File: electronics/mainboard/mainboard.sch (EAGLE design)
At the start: 60 parts, among them CON1 B3B-ZR, IC1 TPS6300, IC2 TPS77033, J1 2MMPAD, J10 2MMPAD, J2 2MMPAD, J3 2MMPAD, J4 2MMPAD, J5 2MMPAD, J6 2MMPAD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

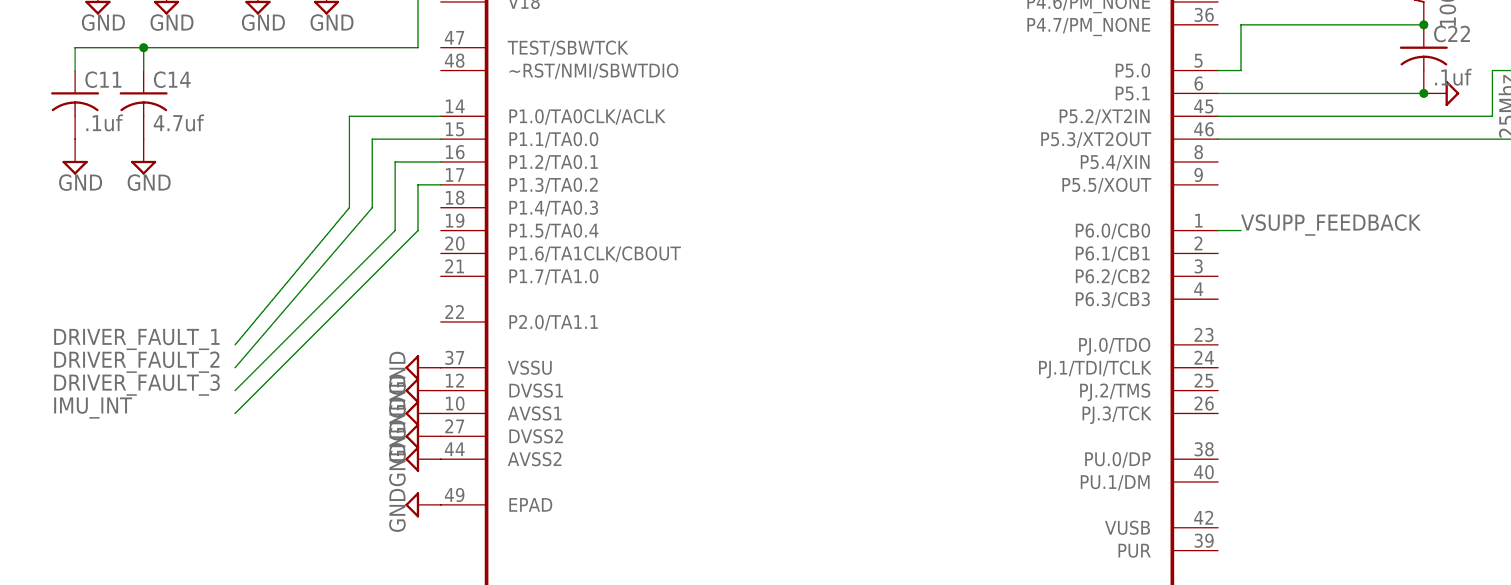
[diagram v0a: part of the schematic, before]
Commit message: renamed some files and cleaned up.  Added motordriver component
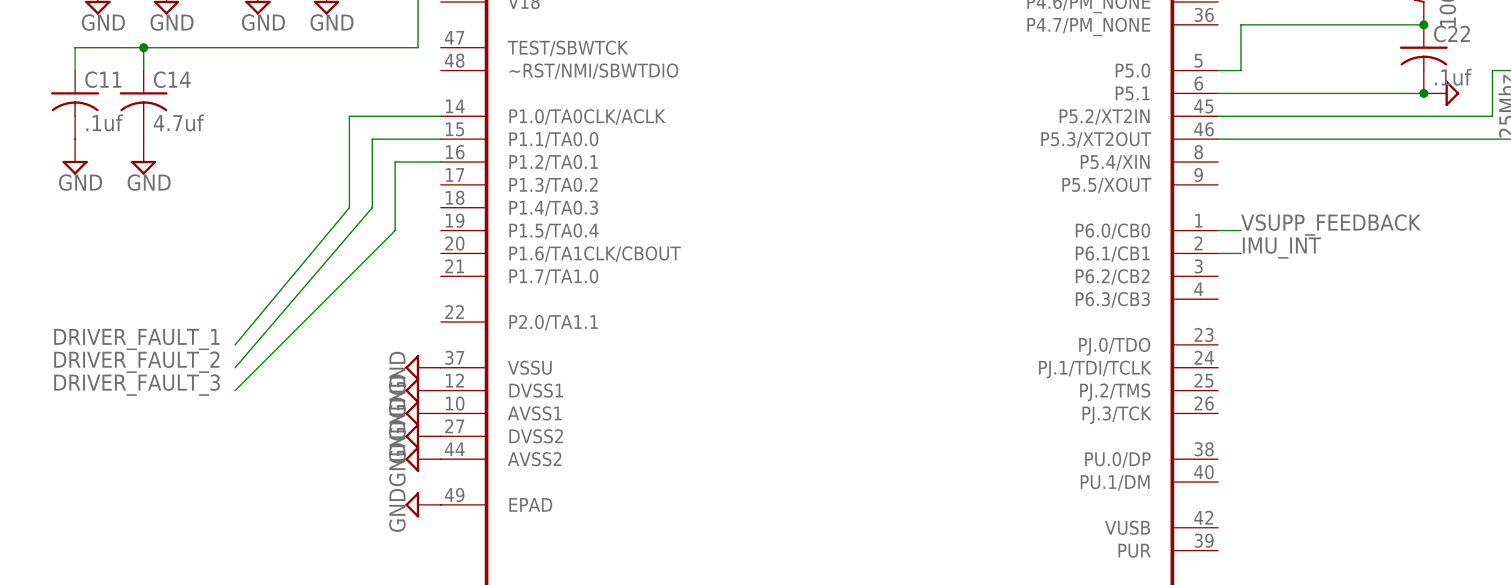
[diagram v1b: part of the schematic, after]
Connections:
- net IMU_INT: now also U2.P6.1/CB1; no longer U2.P1.3/TA0.2
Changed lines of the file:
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@@
 <?xml version="1.0" encoding="utf-8"?>
 <!DOCTYPE eagle SYSTEM "eagle.dtd">
-<eagle version="6.6.0">
+<eagle version="7.0.0">
 <drawing>
 <settings>
@@
 <label x="-12.7" y="-35.56" size="1.778" layer="95"/>
 <pinref part="U2" gate="A" pin="P1.2/TA0.1"/>
-<wire x1="25.4" y1="-10.16" x2="30.48" y2="-10.16" width="0.1524" layer="91"/>
+<wire x1="30.48" y1="-10.16" x2="25.4" y2="-10.16" width="0.1524" layer="91"/>
 </segment>
 </net>
@@
 </segment>
 <segment>
-<wire x1="27.94" y1="-12.7" x2="27.94" y2="-17.78" width="0.1524" layer="91"/>
-<wire x1="27.94" y1="-17.78" x2="7.62" y2="-38.1" width="0.1524" layer="91"/>
-<label x="-12.7" y="-38.1" size="1.778" layer="95"/>
-<pinref part="U2" gate="A" pin="P1.3/TA0.2"/>
-<wire x1="27.94" y1="-12.7" x2="30.48" y2="-12.7" width="0.1524" layer="91"/>
-</segment>
-</net>
+<label x="119.38" y="-20.32" size="1.778" layer="95"/>
+<pinref part="U2" gate="A" pin="P6.1/CB1"/>
+<wire x1="119.38" y1="-20.32" x2="116.84" y2="-20.32" width="0.1524" layer="91"/>
+</segment>
+</net>

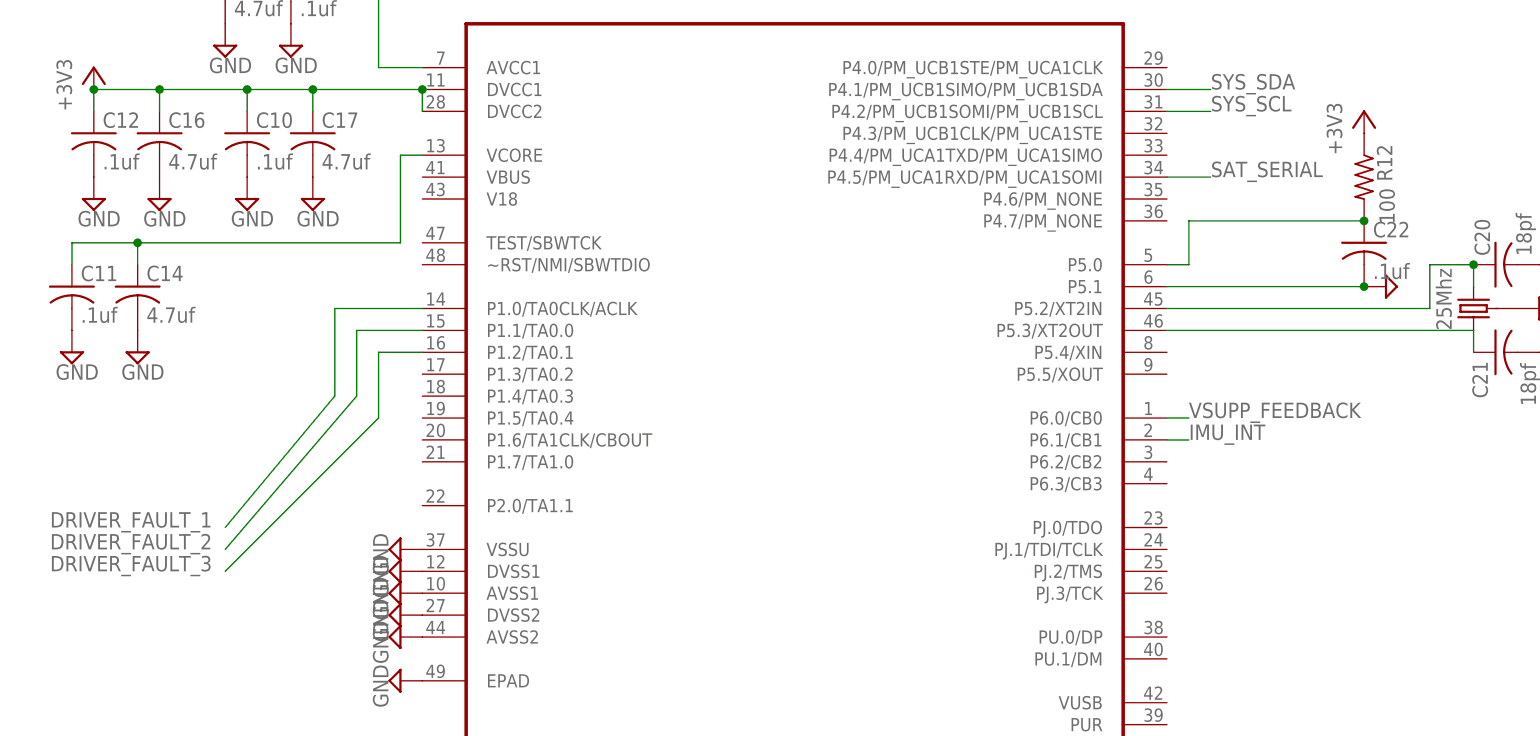
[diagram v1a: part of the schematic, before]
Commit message: layout mostly done, need to add programming header
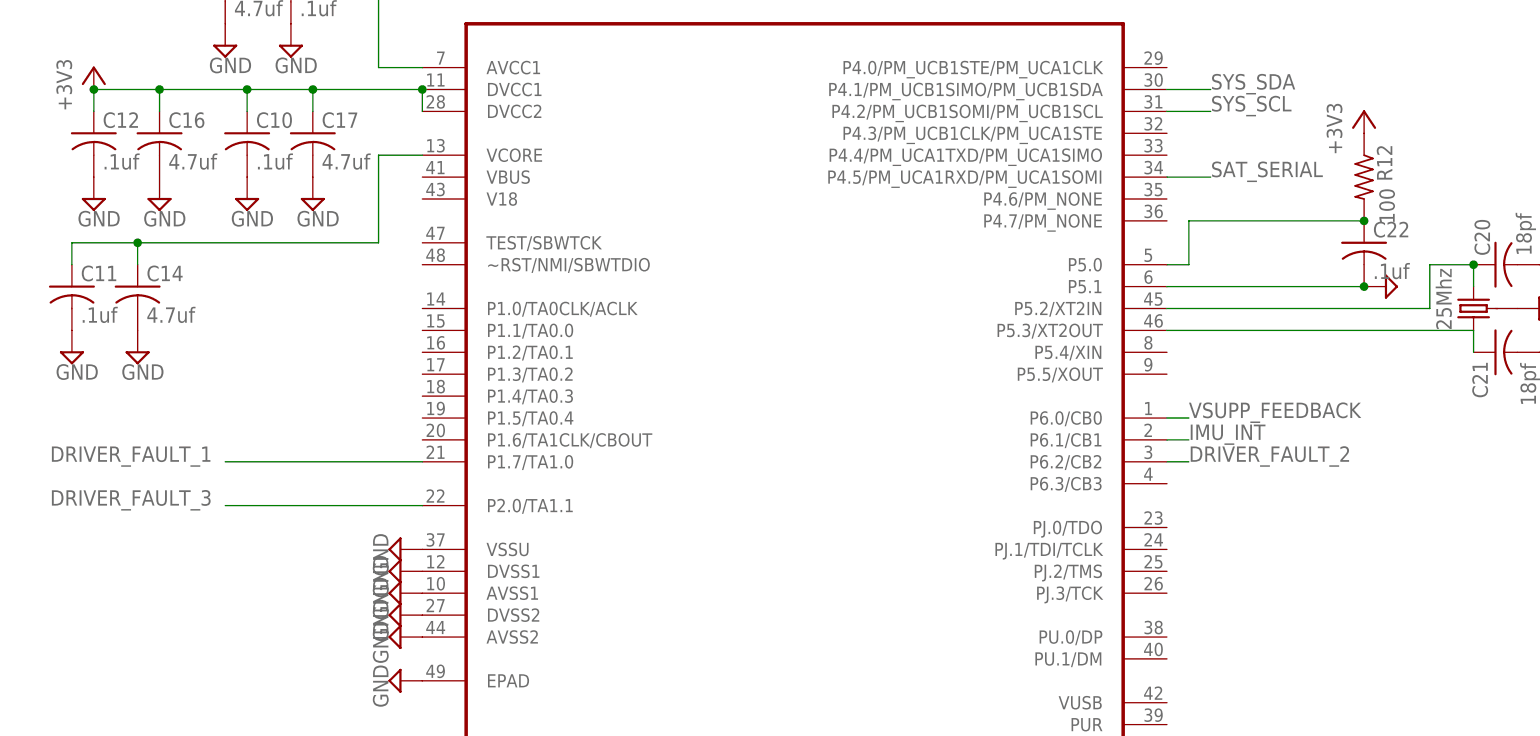
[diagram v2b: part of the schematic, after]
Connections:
- net DRIVER_FAULT_1: now also U2.P1.7/TA1.0; no longer U2.P1.0/TA0CLK/ACLK
- net DRIVER_FAULT_2: now also U2.P6.2/CB2; no longer U2.P1.1/TA0.0
- net DRIVER_FAULT_3: now also U2.P2.0/TA1.1; no longer U2.P1.2/TA0.1
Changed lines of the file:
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@@
 </segment>
 <segment>
-<wire x1="20.32" y1="-5.08" x2="20.32" y2="-15.24" width="0.1524" layer="91"/>
-<wire x1="20.32" y1="-15.24" x2="7.62" y2="-30.48" width="0.1524" layer="91"/>
-<label x="-12.7" y="-30.48" size="1.778" layer="95"/>
-<pinref part="U2" gate="A" pin="P1.0/TA0CLK/ACLK"/>
-<wire x1="30.48" y1="-5.08" x2="20.32" y2="-5.08" width="0.1524" layer="91"/>
+<wire x1="30.48" y1="-22.86" x2="7.62" y2="-22.86" width="0.1524" layer="91"/>
+<label x="-12.7" y="-22.86" size="1.778" layer="95"/>
+<pinref part="U2" gate="A" pin="P1.7/TA1.0"/>
 </segment>
 </net>
@@
 </segment>
 <segment>
-<wire x1="22.86" y1="-7.62" x2="22.86" y2="-15.24" width="0.1524" layer="91"/>
-<wire x1="22.86" y1="-15.24" x2="7.62" y2="-33.02" width="0.1524" layer="91"/>
-<label x="-12.7" y="-33.02" size="1.778" layer="95"/>
-<pinref part="U2" gate="A" pin="P1.1/TA0.0"/>
-<wire x1="30.48" y1="-7.62" x2="22.86" y2="-7.62" width="0.1524" layer="91"/>
+<wire x1="116.84" y1="-22.86" x2="119.38" y2="-22.86" width="0.1524" layer="91"/>
+<label x="119.38" y="-22.86" size="1.778" layer="95"/>
+<pinref part="U2" gate="A" pin="P6.2/CB2"/>
 </segment>
 </net>
@@
 </segment>
 <segment>
-<wire x1="25.4" y1="-10.16" x2="25.4" y2="-17.78" width="0.1524" layer="91"/>
-<wire x1="25.4" y1="-17.78" x2="7.62" y2="-35.56" width="0.1524" layer="91"/>
-<label x="-12.7" y="-35.56" size="1.778" layer="95"/>
-<pinref part="U2" gate="A" pin="P1.2/TA0.1"/>
-<wire x1="30.48" y1="-10.16" x2="25.4" y2="-10.16" width="0.1524" layer="91"/>
+<wire x1="30.48" y1="-27.94" x2="7.62" y2="-27.94" width="0.1524" layer="91"/>
+<label x="-12.7" y="-27.94" size="1.778" layer="95"/>
+<pinref part="U2" gate="A" pin="P2.0/TA1.1"/>
 </segment>
 </net>
@@
 <pinref part="U2" gate="A" pin="VCORE"/>
 <pinref part="C11" gate="G$1" pin="1"/>
-<wire x1="30.48" y1="12.7" x2="27.94" y2="12.7" width="0.1524" layer="91"/>
-<wire x1="27.94" y1="12.7" x2="27.94" y2="2.54" width="0.1524" layer="91"/>
-<wire x1="27.94" y1="2.54" x2="-2.54" y2="2.54" width="0.1524" layer="91"/>
+<wire x1="30.48" y1="12.7" x2="25.4" y2="12.7" width="0.1524" layer="91"/>
+<wire x1="25.4" y1="12.7" x2="25.4" y2="2.54" width="0.1524" layer="91"/>
+<wire x1="25.4" y1="2.54" x2="-2.54" y2="2.54" width="0.1524" layer="91"/>
 <pinref part="C14" gate="G$1" pin="1"/>
 <wire x1="-2.54" y1="0" x2="-2.54" y2="2.54" width="0.1524" layer="91"/>

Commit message: prelim finished board
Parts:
- added J11, J12, J13, J14, J15, J16: ROUND1MM, connectors:ROUND1MM
- added R14: 47k, rcl:R-US_R0402
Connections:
- new net N$24: J11.P$1, U2.PJ.0/TDO
- new net N$25: J12.P$1, U2.PJ.1/TDI/TCLK
- new net N$26: J13.P$1, U2.PJ.2/TMS
- new net N$27: J14.P$1, U2.PJ.3/TCK
- new net N$28: J16.P$1, U2.TEST/SBWTCK
- new net RESET: J15.P$1, R14.2, U2.~RST/NMI/SBWTDIO
- net +3V3: now also R14.1
- net GND: now also U2.VBUS
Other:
- moved on the sheet: C10, C12, C16, C17
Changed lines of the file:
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@@
 <part name="SUPPLY43" library="supply2" deviceset="GND" device=""/>
 <part name="J10" library="connectors" deviceset="2MMPAD" device=""/>
+<part name="SUPPLY47" library="supply2" deviceset="GND" device=""/>
+<part name="R14" library="rcl" deviceset="R-US_" device="R0402" value="47k"/>
+<part name="+3V8" library="supply1" deviceset="+3V3" device=""/>
+<part name="J11" library="connectors" deviceset="ROUND1MM" device=""/>
+<part name="J12" library="connectors" deviceset="ROUND1MM" device=""/>
+<part name="J13" library="connectors" deviceset="ROUND1MM" device=""/>
+<part name="J14" library="connectors" deviceset="ROUND1MM" device=""/>
+<part name="J15" library="connectors" deviceset="ROUND1MM" device=""/>
+<part name="J16" library="connectors" deviceset="ROUND1MM" device=""/>
 </parts>
 <sheets>
@@
 <instance part="SUPPLY24" gate="GND" x="27.94" y="-33.02" rot="R270"/>
 <instance part="SUPPLY25" gate="GND" x="27.94" y="-48.26" rot="R270"/>
-<instance part="C10" gate="G$1" x="10.16" y="15.24"/>
+<instance part="C10" gate="G$1" x="5.08" y="15.24"/>
 <instance part="C11" gate="G$1" x="-10.16" y="-2.54"/>
-<instance part="C12" gate="G$1" x="-7.62" y="15.24"/>
+<instance part="C12" gate="G$1" x="-12.7" y="15.24"/>
 <instance part="SUPPLY27" gate="GND" x="-10.16" y="-10.16"/>
-<instance part="SUPPLY28" gate="GND" x="10.16" y="7.62"/>
-<instance part="SUPPLY29" gate="GND" x="-7.62" y="7.62"/>
-<instance part="+3V2" gate="G$1" x="-7.62" y="22.86"/>
+<instance part="SUPPLY28" gate="GND" x="5.08" y="7.62"/>
+<instance part="SUPPLY29" gate="GND" x="-12.7" y="7.62"/>
+<instance part="+3V2" gate="G$1" x="-12.7" y="22.86"/>
 <instance part="R1" gate="G$1" x="15.24" y="45.72" smashed="yes" rot="R270">
 <attribute name="NAME" x="16.7386" y="49.53" size="1.778" layer="95" rot="R270"/>
@@
 <instance part="SUPPLY31" gate="GND" x="-2.54" y="-10.16"/>
 <instance part="C15" gate="G$1" x="7.62" y="33.02"/>
-<instance part="C16" gate="G$1" x="0" y="15.24"/>
-<instance part="C17" gate="G$1" x="17.78" y="15.24"/>
-<instance part="SUPPLY32" gate="GND" x="17.78" y="7.62"/>
-<instance part="SUPPLY33" gate="GND" x="0" y="7.62"/>
+<instance part="C16" gate="G$1" x="-5.08" y="15.24"/>
+<instance part="C17" gate="G$1" x="12.7" y="15.24"/>
+<instance part="SUPPLY32" gate="GND" x="12.7" y="7.62"/>
+<instance part="SUPPLY33" gate="GND" x="-5.08" y="7.62"/>
 <instance part="SUPPLY34" gate="GND" x="7.62" y="25.4"/>
 <instance part="J1" gate="G$1" x="246.38" y="33.02" smashed="yes">
@@
 <attribute name="NAME" x="-10.16" y="104.14" size="1.778" layer="95" rot="R180"/>
 </instance>
+<instance part="SUPPLY47" gate="GND" x="27.94" y="10.16" rot="R270"/>
+<instance part="R14" gate="G$1" x="17.78" y="-7.62" smashed="yes" rot="R270">
+<attribute name="NAME" x="19.2786" y="-3.81" size="1.778" layer="95" rot="R270"/>
+<attribute name="VALUE" x="19.558" y="-8.89" size="1.778" layer="96" rot="R270"/>
+</instance>
+<instance part="+3V8" gate="G$1" x="17.78" y="0"/>
+<instance part="J11" gate="G$1" x="121.92" y="-30.48"/>
+<instance part="J12" gate="G$1" x="121.92" y="-33.02"/>
+<instance part="J13" gate="G$1" x="121.92" y="-35.56"/>
+<instance part="J14" gate="G$1" x="121.92" y="-38.1"/>
+<instance part="J15" gate="G$1" x="10.16" y="-15.24" rot="R180"/>
+<instance part="J16" gate="G$1" x="25.4" y="2.54" rot="R180"/>
 </instances>
 <busses>
@@
 <pinref part="C25" gate="G$1" pin="2"/>
 <pinref part="SUPPLY43" gate="GND" pin="GND"/>
+</segment>
+<segment>
+<pinref part="U2" gate="A" pin="VBUS"/>
+<pinref part="SUPPLY47" gate="GND" pin="GND"/>
 </segment>
 </net>
@@
 <pinref part="U2" gate="A" pin="DVCC1"/>
 <pinref part="C12" gate="G$1" pin="1"/>
-<wire x1="30.48" y1="20.32" x2="17.78" y2="20.32" width="0.1524" layer="91"/>
+<wire x1="30.48" y1="20.32" x2="12.7" y2="20.32" width="0.1524" layer="91"/>
 <pinref part="+3V2" gate="G$1" pin="+3V3"/>
-<wire x1="17.78" y1="20.32" x2="10.16" y2="20.32" width="0.1524" layer="91"/>
-<wire x1="10.16" y1="20.32" x2="0" y2="20.32" width="0.1524" layer="91"/>
-<wire x1="0" y1="17.78" x2="0" y2="20.32" width="0.1524" layer="91"/>
-<wire x1="0" y1="20.32" x2="-7.62" y2="20.32" width="0.1524" layer="91"/>
+<wire x1="12.7" y1="20.32" x2="5.08" y2="20.32" width="0.1524" layer="91"/>
+<wire x1="5.08" y1="20.32" x2="-5.08" y2="20.32" width="0.1524" layer="91"/>
+<wire x1="-5.08" y1="17.78" x2="-5.08" y2="20.32" width="0.1524" layer="91"/>
+<wire x1="-5.08" y1="20.32" x2="-12.7" y2="20.32" width="0.1524" layer="91"/>
 <pinref part="C10" gate="G$1" pin="1"/>
-<wire x1="10.16" y1="17.78" x2="10.16" y2="20.32" width="0.1524" layer="91"/>
-<junction x="10.16" y="20.32"/>
+<wire x1="5.08" y1="17.78" x2="5.08" y2="20.32" width="0.1524" layer="91"/>
+<junction x="5.08" y="20.32"/>
 <pinref part="C16" gate="G$1" pin="1"/>
 <pinref part="U2" gate="A" pin="DVCC2"/>
 <wire x1="30.48" y1="17.78" x2="30.48" y2="20.32" width="0.1524" layer="91"/>
 <pinref part="C17" gate="G$1" pin="1"/>
-<wire x1="17.78" y1="17.78" x2="17.78" y2="20.32" width="0.1524" layer="91"/>
+<wire x1="12.7" y1="17.78" x2="12.7" y2="20.32" width="0.1524" layer="91"/>
 <junction x="30.48" y="20.32"/>
-<junction x="17.78" y="20.32"/>
-<wire x1="-7.62" y1="17.78" x2="-7.62" y2="20.32" width="0.1524" layer="91"/>
-<junction x="-7.62" y="20.32"/>
-<junction x="0" y="20.32"/>
+<junction x="12.7" y="20.32"/>
+<wire x1="-12.7" y1="17.78" x2="-12.7" y2="20.32" width="0.1524" layer="91"/>
+<junction x="-12.7" y="20.32"/>
+<junction x="-5.08" y="20.32"/>
 </segment>
 <segment>
@@
 <wire x1="241.3" y1="101.6" x2="246.38" y2="101.6" width="0.1524" layer="91"/>
 <wire x1="246.38" y1="101.6" x2="246.38" y2="106.68" width="0.1524" layer="91"/>
+</segment>
+<segment>
+<pinref part="R14" gate="G$1" pin="1"/>
+<pinref part="+3V8" gate="G$1" pin="+3V3"/>
 </segment>
 </net>
@@
 <pinref part="U2" gate="A" pin="VCORE"/>
 <pinref part="C11" gate="G$1" pin="1"/>
-<wire x1="30.48" y1="12.7" x2="25.4" y2="12.7" width="0.1524" layer="91"/>
-<wire x1="25.4" y1="12.7" x2="25.4" y2="2.54" width="0.1524" layer="91"/>
-<wire x1="25.4" y1="2.54" x2="-2.54" y2="2.54" width="0.1524" layer="91"/>
+<wire x1="30.48" y1="12.7" x2="20.32" y2="12.7" width="0.1524" layer="91"/>
+<wire x1="20.32" y1="12.7" x2="20.32" y2="2.54" width="0.1524" layer="91"/>
+<wire x1="20.32" y1="2.54" x2="-2.54" y2="2.54" width="0.1524" layer="91"/>
 <pinref part="C14" gate="G$1" pin="1"/>
 <wire x1="-2.54" y1="0" x2="-2.54" y2="2.54" width="0.1524" layer="91"/>
@@
 <pinref part="C21" gate="G$1" pin="1"/>
 <wire x1="152.4" y1="-10.16" x2="152.4" y2="-7.62" width="0.1524" layer="91"/>
+<junction x="152.4" y="-7.62"/>
 </segment>
 </net>
@@
 </segment>
 </net>
+<net name="RESET" class="0">
+<segment>
+<pinref part="U2" gate="A" pin="~RST/NMI/SBWTDIO"/>
+<wire x1="30.48" y1="0" x2="22.86" y2="0" width="0.1524" layer="91"/>
+<wire x1="22.86" y1="0" x2="22.86" y2="-15.24" width="0.1524" layer="91"/>
+<pinref part="R14" gate="G$1" pin="2"/>
+<wire x1="22.86" y1="-15.24" x2="17.78" y2="-15.24" width="0.1524" layer="91"/>
+<wire x1="17.78" y1="-15.24" x2="17.78" y2="-12.7" width="0.1524" layer="91"/>
+<wire x1="17.78" y1="-15.24" x2="15.24" y2="-15.24" width="0.1524" layer="91"/>
+<label x="7.62" y="-15.24" size="1.778" layer="95" rot="R180"/>
+<pinref part="J15" gate="G$1" pin="P$1"/>
+<junction x="17.78" y="-15.24"/>
+</segment>
+</net>
+<net name="N$24" class="0">
+<segment>
+<pinref part="U2" gate="A" pin="PJ.0/TDO"/>
+<pinref part="J11" gate="G$1" pin="P$1"/>
+</segment>
+</net>
+<net name="N$25" class="0">
+<segment>
+<pinref part="U2" gate="A" pin="PJ.1/TDI/TCLK"/>
+<pinref part="J12" gate="G$1" pin="P$1"/>
+</segment>
+</net>
+<net name="N$26" class="0">
+<segment>
+<pinref part="U2" gate="A" pin="PJ.2/TMS"/>
+<pinref part="J13" gate="G$1" pin="P$1"/>
+</segment>
+</net>
+<net name="N$27" class="0">
+<segment>
+<pinref part="U2" gate="A" pin="PJ.3/TCK"/>
+<pinref part="J14" gate="G$1" pin="P$1"/>
+</segment>
+</net>
+<net name="N$28" class="0">
+<segment>
+<pinref part="U2" gate="A" pin="TEST/SBWTCK"/>
+<pinref part="J16" gate="G$1" pin="P$1"/>
+</segment>
+</net>
